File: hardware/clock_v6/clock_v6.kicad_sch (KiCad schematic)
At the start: 241 parts, among them J1 RJ45, J12 Conn_01x06, J2 Conn_01x06_Pin, J3 Conn_01x05_Pin, J4 Conn_01x04_Pin, J5 Conn_01x06_Pin, J6 Conn_01x04_Pin, J7 Conn_01x04_Pin, J8 Conn_01x02, J9 Conn_02x10_Odd_Even, Q1 2N7002, Q10 2N7002, Q2 2N7002, Q3 2N7002, Q4 2N7002, Q5 2N7002, Q6 2N7002, Q7 2N7002, Q8 2N7002, Q9 2N7002, U1 ADA4807-1, U10 STM32F405RGTx, U11 AMS1117-3.3, U12 BA50DD0WHFP-TR, U13 M24C02-RMN, U2 SN74LVC1G14DBV, U3 SN74LVC1G14DBV, U4 ADA4807-1, U5 ADA4807-1, U6 TLV3603DCKR, U7 SN74LVC1G14DBV, U8 TLV3603DCKR, U9 L78L05_SOT89, X2 GTXO-14V (2.048MHz), Y1 AOCJY4A-10.000MHZ-SW, Y2 16MHz

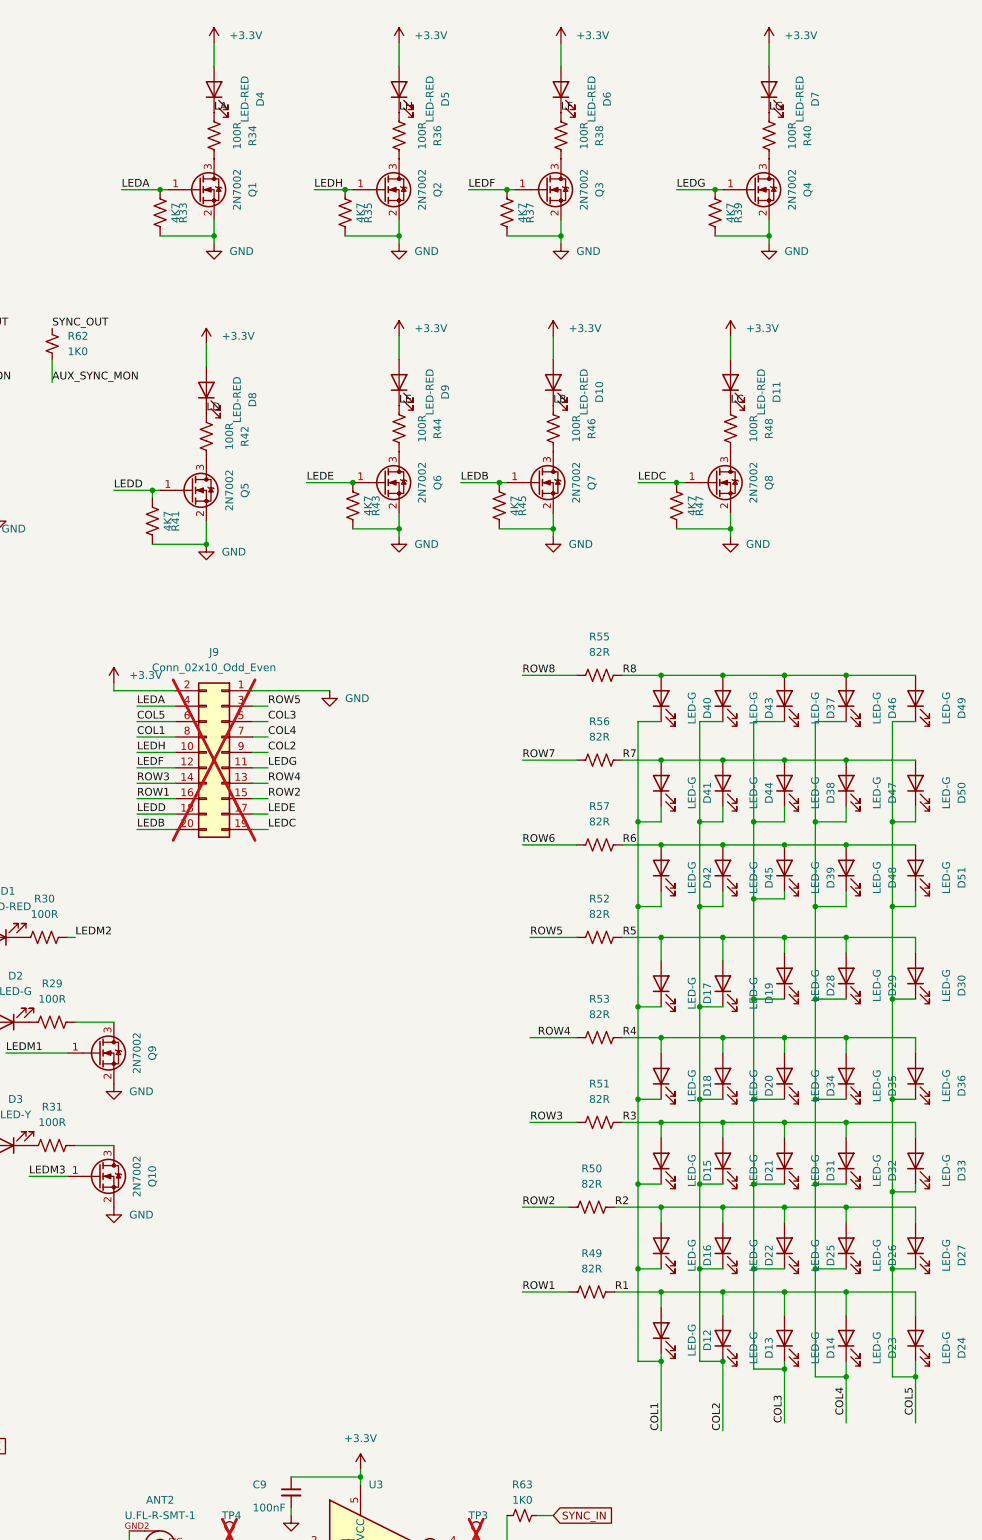
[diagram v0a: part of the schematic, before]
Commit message: start cleaning up clock PCB
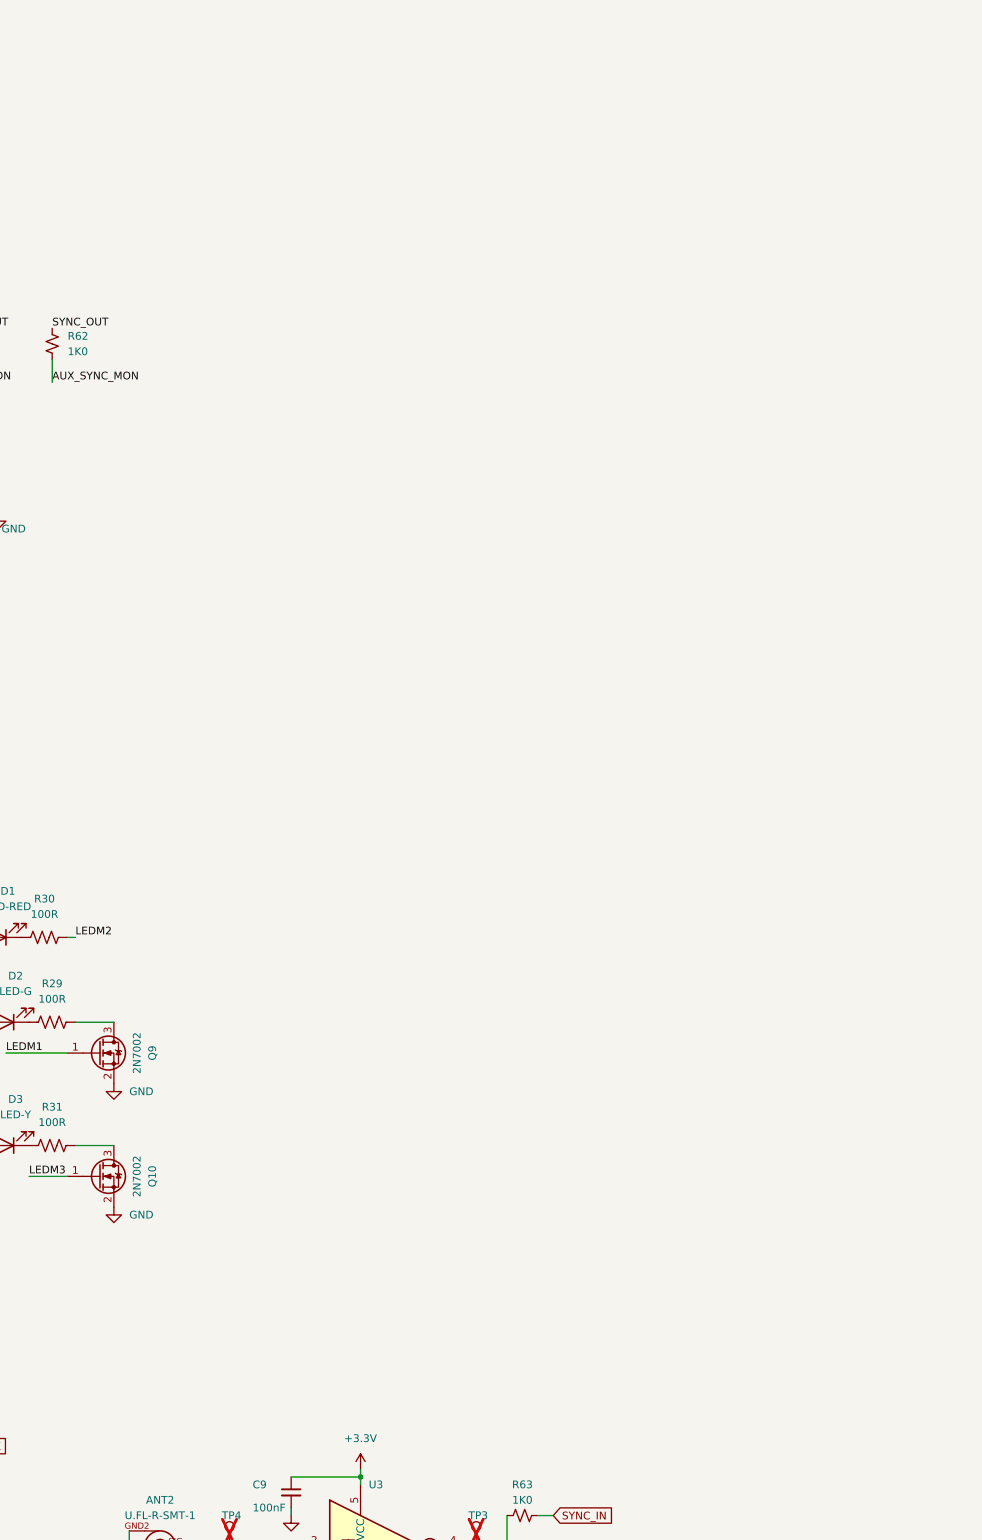
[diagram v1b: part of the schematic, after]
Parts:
- removed D10, D11, D4, D5, D6, D7, D8, D9: LED-RED, LED_SMD:LED_0603_1608Metric, symbol Device:LED
- removed D12, D13, D14, D15, D16, D17, D18, D19, D20, D21, D22, D23, D24, D25, D26, D27, D28, D29, D30, D31, D32, D33, D34, D35, D36, D37, D38, D39, D40, D41, D42, D43, D44, D45, D46, D47, D48, D49, D50, D51: LED-G, LED_SMD:LED_0603_1608Metric, symbol Device:LED
- removed J9: Conn_02x10_Odd_Even, Connector_PinHeader_2.54mm:PinHeader_2x10_P2.54mm_Vertical, symbol Connector_Generic:Conn_02x10_Odd_Even
- removed Q1, Q2, Q3, Q4, Q5, Q6, Q7, Q8: 2N7002, Package_TO_SOT_SMD:SOT-23, symbol Transistor_FET:2N7002
- removed R33, R35, R37, R39, R41, R43, R45, R47: 4K7, Resistor_SMD:R_0603_1608Metric, symbol Device:R_US
- removed R34, R36, R38, R40, R42, R44, R46, R48: 100R, Resistor_SMD:R_0603_1608Metric, symbol Device:R_US
- removed R49, R50, R51, R52, R53, R55, R56, R57: 82R, Resistor_SMD:R_0603_1608Metric, symbol Device:R_US

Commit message: reduce schematic paper size
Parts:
- removed ANT6: U.FL-R-SMT-1, blinky_footprints:U.FL-R-SMT-1, symbol blinky:U.FL-R-SMT-1
- removed J3: Conn_01x05_Pin, Connector_PinHeader_2.54mm:PinHeader_1x05_P2.54mm_Vertical, symbol Connector:Conn_01x05_Pin
- removed JP1: SolderJumper_2_Bridged, Jumper:SolderJumper-2_P1.3mm_Bridged_RoundedPad1.0x1.5mm, symbol Jumper:SolderJumper_2_Bridged
- removed RV1: 20K, Potentiometer_SMD:Potentiometer_Bourns_3314G_Vertical, symbol Device:R_Potentiometer_US
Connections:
- net Vadj: now also R12.2, R13.1, R23.2
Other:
- title: Blinky V4 -> Clock V6
- moved on the sheet: ANT1, ANT2, ANT3, ANT4, ANT5, C1, C10, C11, C12, C13, C14, C15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

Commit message: dreive new ros off of boot0 boot1
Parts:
- removed TP12, TP13, TP14: ~, TestPoint:TestPoint_THTPad_D1.5mm_Drill0.7mm, symbol Connector:TestPoint
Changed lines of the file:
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@@
   (junction (at 204.47 162.56) (diameter 0) (color 0 0 0 0)
   )
-  (junction (at 167.64 36.83) (diameter 0) (color 0 0 0 0)
-  )
   (junction (at 309.88 66.04) (diameter 0) (color 0 0 0 0)
   )
@@
   (junction (at 303.53 166.37) (diameter 0) (color 0 0 0 0)
   )
-  (junction (at 153.67 29.21) (diameter 0) (color 0 0 0 0)
-  )
   (junction (at 213.36 226.06) (diameter 0) (color 0 0 0 0)
   )
@@
   (junction (at 21.59 250.19) (diameter 0) (color 0 0 0 0)
   )
-  (junction (at 227.33 81.28) (diameter 0) (color 0 0 0 0)
-  )
   (junction (at 312.42 140.97) (diameter 0) (color 0 0 0 0)
   )
@@
     (stroke (width 0) (type default))
   )
-  (wire (pts (xy 153.67 29.21) (xy 177.8 29.21))
-    (stroke (width 0) (type default))
-  )
   (wire (pts (xy 213.36 218.44) (xy 213.36 219.71))
     (stroke (width 0) (type default))
@@
     (stroke (width 0) (type default))
   )
-  (wire (pts (xy 153.67 29.21) (xy 144.78 29.21))
+  (wire (pts (xy 144.78 29.21) (xy 177.8 29.21))
     (stroke (width 0) (type default))
   )
@@
     (stroke (width 0) (type default))
   )
-  (wire (pts (xy 227.33 81.28) (xy 228.6 81.28))
+  (wire (pts (xy 213.36 81.28) (xy 228.6 81.28))
     (stroke (width 0) (type default))
   )
@@
     (stroke (width 0) (type default))
   )
-  (wire (pts (xy 167.64 35.56) (xy 167.64 36.83))
-    (stroke (width 0) (type default))
-  )
   (wire (pts (xy 134.62 53.34) (xy 139.7 53.34))
     (stroke (width 0) (type default))
@@
   )
   (wire (pts (xy 377.19 217.17) (xy 379.73 217.17))
-    (stroke (width 0) (type default))
-  )
-  (wire (pts (xy 213.36 81.28) (xy 227.33 81.28))
     (stroke (width 0) (type default))
   )
@@
     )
   )
-  (symbol (lib_id "Connector:TestPoint") (at 153.67 29.21 0) (unit 1)
-    (in_bom no) (on_board yes) (dnp yes) (fields_autoplaced)
-    (property "Reference" "TP12" (at 156.21 25.908 0)
-      (effects (font (size 1.27 1.27)) (justify left))
-    )
-    (property "Value" "~" (at 156.21 27.178 0)
-      (effects (font (size 1.27 1.27)) (justify left))
-    )
-    (property "Footprint" "TestPoint:TestPoint_THTPad_D1.5mm_Drill0.7mm" (at 158.75 29.21 0)
-      (effects (font (size 1.27 1.27)) hide)
-    )
-    (property "Datasheet" "~" (at 158.75 29.21 0)
-      (effects (font (size 1.27 1.27)) hide)
-    )
-    (pin "1")
-    (instances
-      (project "clock_v6"
-        (path "/bd4d3b9a-07c1-4a53-9c94-2893f3e869d4"
-          (reference "TP12") (unit 1)
-        )
-      )
-    )
-  )
   (symbol (lib_id "Device:C_Small") (at 364.49 173.99 0) (unit 1)
     (in_bom yes) (on_board yes) (dnp no)
@@
         (path "/bd4d3b9a-07c1-4a53-9c94-2893f3e869d4"
           (reference "#PWR051") (unit 1)
-        )
-      )
-    )
-  )
-  (symbol (lib_id "Connector:TestPoint") (at 167.64 35.56 0) (unit 1)
-    (in_bom no) (on_board yes) (dnp yes)
-    (property "Reference" "TP13" (at 162.56 31.75 0)
-      (effects (font (size 1.27 1.27)) (justify left))
-    )
-    (property "Value" "~" (at 170.18 33.528 0)
-      (effects (font (size 1.27 1.27)) (justify left))
-    )
-    (property "Footprint" "TestPoint:TestPoint_THTPad_D1.5mm_Drill0.7mm" (at 172.72 35.56 0)
-      (effects (font (size 1.27 1.27)) hide)
-    )
-    (property "Datasheet" "~" (at 172.72 35.56 0)
-      (effects (font (size 1.27 1.27)) hide)
-    )
-    (pin "1")
-    (instances
-      (project "clock_v6"
-        (path "/bd4d3b9a-07c1-4a53-9c94-2893f3e869d4"
-          (reference "TP13") (unit 1)
         )
       )
@@
         )
       )
-    )
-  )
-  (symbol (lib_id "Connector:TestPoint") (at 227.33 81.28 0) (unit 1)
-    (in_bom no) (on_board yes) (dnp yes)
-    (property "Reference" "TP14" (at 226.06 76.2 0)
-      (effects (font (size 1.27 1.27)) (justify left))
-    )
-    (property "Value" "~" (at 229.87 79.248 0)
-      (effects (font (size 1.27 1.27)) (justify left))
-    )
-    (property "Footprint" "TestPoint:TestPoint_THTPad_D1.5mm_Drill0.7mm" (at 232.41 81.28 0)
-      (effects (font (size 1.27 1.27)) hide)
-    )
-    (property "Datasheet" "~" (at 232.41 81.28 0)
-      (effects (font (size 1.27 1.27)) hide)
-    )
-    (pin "1")
-    (instances
-      (project "clock_v6"
-        (path "/bd4d3b9a-07c1-4a53-9c94-2893f3e869d4"
-          (reference "TP14") (unit 1)
-        )
-      )

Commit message: remove cheap osc
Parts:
- removed TP11: ~, TestPoint:TestPoint_THTPad_D1.5mm_Drill0.7mm, symbol Connector:TestPoint
- removed X2: GTXO-14V (2.048MHz), Oscillator:Oscillator_DIP-14, symbol Oscillator:GTXO-14V
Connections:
- net AUX_CLK: no longer TP10.1, U7.4
- net CLK: now also TP10.1, U7.4
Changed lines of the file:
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@@
   (junction (at 320.04 66.04) (diameter 0) (color 0 0 0 0)
   )
-  (junction (at 284.48 120.65) (diameter 0) (color 0 0 0 0)
-  )
   (junction (at 33.02 247.65) (diameter 0) (color 0 0 0 0)
   )
@@
     (stroke (width 0) (type default))
   )
-  (wire (pts (xy 284.48 120.65) (xy 290.83 120.65))
+  (wire (pts (xy 270.51 120.65) (xy 290.83 120.65))
     (stroke (width 0) (type default))
   )
@@
     (stroke (width 0) (type default))
   )
-  (wire (pts (xy 270.51 120.65) (xy 284.48 120.65))
-    (stroke (width 0) (type default))
-  )
   (wire (pts (xy 129.54 45.72) (xy 129.54 53.34))
     (stroke (width 0) (type default))
@@
     (stroke (width 0) (type default))
   )
-  (wire (pts (xy 284.48 119.38) (xy 284.48 120.65))
-    (stroke (width 0) (type default))
-  )
   (wire (pts (xy 328.93 204.47) (xy 323.85 204.47))
     (stroke (width 0) (type default))
@@
     (effects (font (size 1.27 1.27)) (justify left bottom))
   )
-  (label "CLK" (at 92.71 105.41 0) (fields_autoplaced)
-    (effects (font (size 1.27 1.27)) (justify left bottom))
-  )
   (label "SDA" (at 134.62 110.49 270) (fields_autoplaced)
     (effects (font (size 1.27 1.27)) (justify right bottom))
@@
     (effects (font (size 1.27 1.27)) (justify left bottom))
   )
-  (label "OSC_ADJ" (at 72.39 105.41 180) (fields_autoplaced)
-    (effects (font (size 1.27 1.27)) (justify right bottom))
-  )
   (label "USB_RX" (at 113.03 82.55 0) (fields_autoplaced)
     (effects (font (size 1.27 1.27)) (justify left bottom))
@@
     )
   )
-  (global_label "AUX_CLK" (shape input) (at 403.86 77.47 0) (fields_autoplaced)
+  (global_label "CLK" (shape input) (at 403.86 77.47 0) (fields_autoplaced)
     (effects (font (size 1.27 1.27)) (justify left))
-    (property "Intersheetrefs" "${INTERSHEET_REFS}" (at 414.9301 77.47 0)
+    (property "Intersheetrefs" "${INTERSHEET_REFS}" (at 410.3339 77.47 0)
       (effects (font (size 1.27 1.27)) (justify left) hide)
     )
@@
     )
   )
-  (symbol (lib_id "power:GND") (at 85.09 113.03 0) (unit 1)
-    (in_bom yes) (on_board yes) (dnp no) (fields_autoplaced)
-    (property "Reference" "#PWR0108" (at 85.09 119.38 0)
-      (effects (font (size 1.27 1.27)) hide)
-    )
-    (property "Value" "GND" (at 85.09 118.11 0)
-      (effects (font (size 1.27 1.27)))
-    )
-    (property "Footprint" "" (at 85.09 113.03 0)
-      (effects (font (size 1.27 1.27)) hide)
-    )
-    (property "Datasheet" "" (at 85.09 113.03 0)
-      (effects (font (size 1.27 1.27)) hide)
-    )
-    (pin "1")
-    (instances
-      (project "clock_v6"
-        (path "/bd4d3b9a-07c1-4a53-9c94-2893f3e869d4"
-          (reference "#PWR0108") (unit 1)
-        )
-      )
-    )
-  )
   (symbol (lib_id "Mechanical:MountingHole") (at 44.45 109.22 0) (unit 1)
     (in_bom no) (on_board yes) (dnp yes) (fields_autoplaced)
@@
     )
   )
-  (symbol (lib_id "power:+3.3V") (at 85.09 97.79 0) (unit 1)
-    (in_bom yes) (on_board yes) (dnp no) (fields_autoplaced)
-    (property "Reference" "#PWR0109" (at 85.09 101.6 0)
-      (effects (font (size 1.27 1.27)) hide)
-    )
-    (property "Value" "+3.3V" (at 85.09 92.71 0)
-      (effects (font (size 1.27 1.27)))
-    )
-    (property "Footprint" "" (at 85.09 97.79 0)
-      (effects (font (size 1.27 1.27)) hide)
-    )
-    (property "Datasheet" "" (at 85.09 97.79 0)
-      (effects (font (size 1.27 1.27)) hide)
-    )
-    (pin "1")
-    (instances
-      (project "clock_v6"
-        (path "/bd4d3b9a-07c1-4a53-9c94-2893f3e869d4"
-          (reference "#PWR0109") (unit 1)
-        )
-      )
-    )
-  )
   (symbol (lib_id "Device:R_Small_US") (at 346.71 128.27 90) (unit 1)
     (in_bom yes) (on_board yes) (dnp no) (fields_autoplaced)
@@
     )
   )
-  (symbol (lib_id "Connector:TestPoint") (at 284.48 119.38 0) (unit 1)
-    (in_bom no) (on_board yes) (dnp yes)
-    (property "Reference" "TP11" (at 283.21 114.3 0)
-      (effects (font (size 1.27 1.27)) (justify left))
-    )
-    (property "Value" "~" (at 287.02 117.348 0)
-      (effects (font (size 1.27 1.27)) (justify left) hide)
-    )
-    (property "Footprint" "TestPoint:TestPoint_THTPad_D1.5mm_Drill0.7mm" (at 289.56 119.38 0)
-      (effects (font (size 1.27 1.27)) hide)
-    )
-    (property "Datasheet" "~" (at 289.56 119.38 0)
-      (effects (font (size 1.27 1.27)) hide)
-    )
-    (pin "1")
-    (instances
-      (project "clock_v6"
-        (path "/bd4d3b9a-07c1-4a53-9c94-2893f3e869d4"
-          (reference "TP11") (unit 1)
-        )
-      )
-    )
-  )
   (symbol (lib_id "blinky:U.FL-R-SMT-1") (at 406.4 168.91 0) (unit 1)
     (in_bom yes) (on_board yes) (dnp no)
@@
         )
       )
-    )
-  )
-  (symbol (lib_id "Oscillator:GTXO-14V") (at 85.09 105.41 0) (unit 1)
-    (in_bom no) (on_board yes) (dnp yes)
-    (property "Reference" "X2" (at 88.9 97.79 0)
-      (effects (font (size 1.27 1.27)))
-    )
-    (property "Value" "GTXO-14V (2.048MHz)" (at 71.12 97.79 0)
-      (effects (font (size 1.27 1.27)))
-    )
-    (property "Footprint" "Oscillator:Oscillator_DIP-14" (at 96.52 114.3 0)
-      (effects (font (size 1.27 1.27)) hide)
-    )
-    (property "Datasheet" "http://www.golledge.com/pdf/products/tcxos/gtxo14.pdf" (at 77.47 102.87 0)
-      (effects (font (size 1.27 1.27)) hide)
-    )
-    (pin "1")
-    (pin "14")
-    (pin "7")
-    (pin "8")
-    (instances
-      (project "clock_v6"
-        (path "/bd4d3b9a-07c1-4a53-9c94-2893f3e869d4"
-          (reference "X2") (unit 1)
-        )
-      )

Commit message: clean up connections and add gps tx voltage dividers
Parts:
- removed TP1, TP18: ~, TestPoint:TestPoint_THTPad_D1.5mm_Drill0.7mm, symbol Connector:TestPoint
- added R33, R35: 2K2, Resistor_SMD:R_0603_1608Metric, symbol Device:R_US
- added R34, R36: 4K7, Resistor_SMD:R_0603_1608Metric, symbol Device:R_US
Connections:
- net GND: now also R34.1, R36.1
- net GPS_TX1: now also R35.1, R36.2; no longer J1.5, J2.3 (Pin_3)
- net GPS_TX2: now also R33.1, R34.2; no longer J1.8, J2.6 (Pin_6)
- new net GPS_TX1H: J1.5, J2.3 (Pin_3), R35.2
- new net GPS_TX2H: J1.8, J2.6 (Pin_6), R33.2
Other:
- moved on the sheet: J2

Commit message: add BNC connectors to clock board
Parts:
- removed TP15, TP2, TP3, TP4, TP5, TP6, TP7: ~, TestPoint:TestPoint_THTPad_D1.5mm_Drill0.7mm, symbol Connector:TestPoint
- added J? (x5): KH-BNC50-3511, blinky_footprints:BNC_Amphenol_B6252HB-NPP3G-50_Horizontal-CJ, symbol Connector:Conn_Coaxial
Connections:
- net GND: now also J?.2 (Ext), J?.2 (Ext), J?.2 (Ext), J?.2 (Ext), J?.2 (Ext)
- net at ANT1.SIG, C4.2, R4.2: now also J?.1 (In)
- net at ANT3.SIG, C7.2, L2.1: now also J?.1 (In)
- net at ANT5.SIG, C23.2, L6.1: now also J?.1 (In)
- net at ANT2.SIG, R5.1, U3.2: now also J?.1 (In)
- net at ANT4.SIG, C14.2, L4.1: now also J?.1 (In)
